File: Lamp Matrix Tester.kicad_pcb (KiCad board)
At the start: 2 copper layers, 50.8 x 53.3 mm, 11 parts, among them J1 Columns, J2 Rows, U1 1088AS

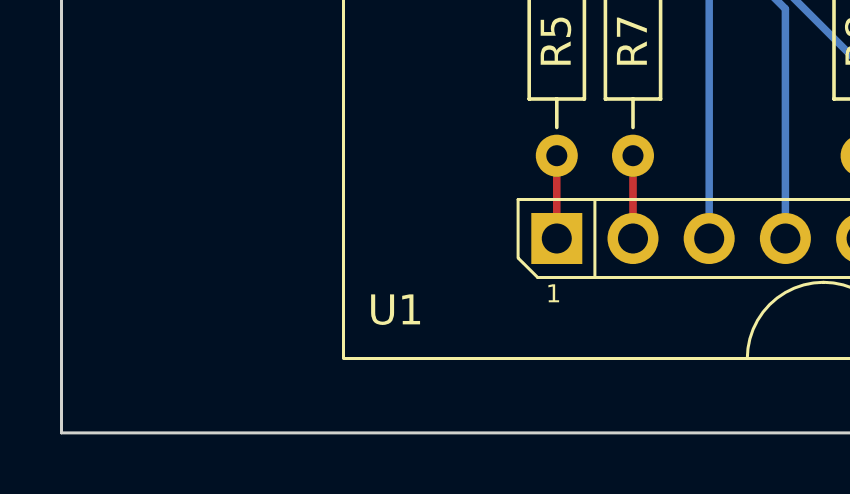
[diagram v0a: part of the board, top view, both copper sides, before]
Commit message: Migrate to Kicad 8 + Included symbol/footprint and 3D model for 1088AS module
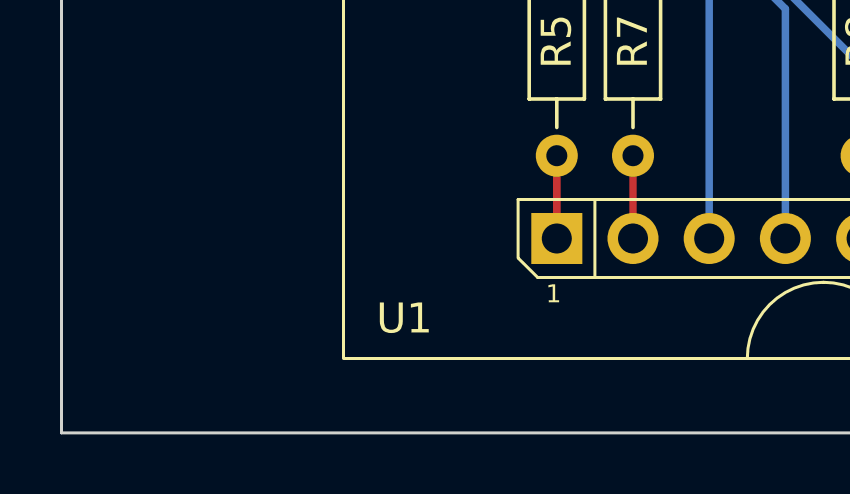
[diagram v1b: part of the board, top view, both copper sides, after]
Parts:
- U1: footprint Library:Led_1088AS_8x8_P2.54mm -> LampMatrixTesterLibrary:Led_1088AS_8x8_P2.54mm
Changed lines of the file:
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@@
     )
   )
-  (footprint "Library:Led_1088AS_8x8_P2.54mm" locked (layer "F.Cu")
+  (footprint "LampMatrixTesterLibrary:Led_1088AS_8x8_P2.54mm" (layer "F.Cu")
     (at 48.26 50.1)
     (descr "8x8 Led matrix module (rows on cathodes)")
@@
     (property "Sheetname" "")
     (attr through_hole)
-    (fp_text reference "U1" (at -14.26 14.4) (layer "F.SilkS")
+    (fp_text reference "U1" (at -13.97 14.67) (layer "F.SilkS")
         (effects (font (size 1 1) (thickness 0.15)))
     )
@@
         (effects (font (size 1 1) (thickness 0.15)))
     )
-    (fp_text user "U1" (at 0 0 180) (layer "F.Fab")
+    (fp_text user "${REFERENCE}" (at 10.16 -17.78 180) (layer "F.Fab")
         (effects (font (size 1 1) (thickness 0.15)))
     )
@@
     (fp_line (start 10.16 13.27) (end -9.525 13.27)
       (stroke (width 0.1) (type solid)) (layer "F.Fab"))
-    (pad "1" thru_hole rect locked (at -8.89 12) (size 1.7 1.7) (drill 1) (layers "*.Cu" "*.Mask")
+    (pad "1" thru_hole rect (at -8.89 12) (size 1.7 1.7) (drill 1) (layers "*.Cu" "*.Mask")
       (net 21 "Net-(U1-R5)") (pinfunction "R5") (pintype "input"))
-    (pad "2" thru_hole oval locked (at -6.35 12) (size 1.7 1.7) (drill 1) (layers "*.Cu" "*.Mask")
+    (pad "2" thru_hole oval (at -6.35 12) (size 1.7 1.7) (drill 1) (layers "*.Cu" "*.Mask")
       (net 23 "Net-(U1-R7)") (pinfunction "R7") (pintype "input"))
-    (pad "3" thru_hole oval locked (at -3.81 12) (size 1.7 1.7) (drill 1) (layers "*.Cu" "*.Mask")
+    (pad "3" thru_hole oval (at -3.81 12) (size 1.7 1.7) (drill 1) (layers "*.Cu" "*.Mask")
       (net 2 "/Col_2") (pinfunction "C2") (pintype "input"))
-    (pad "4" thru_hole oval locked (at -1.27 12) (size 1.7 1.7) (drill 1) (layers "*.Cu" "*.Mask")
+    (pad "4" thru_hole oval (at -1.27 12) (size 1.7 1.7) (drill 1) (layers "*.Cu" "*.Mask")
       (net 3 "/Col_3") (pinfunction "C3") (pintype "input"))
-    (pad "5" thru_hole oval locked (at 1.27 12) (size 1.7 1.7) (drill 1) (layers "*.Cu" "*.Mask")
+    (pad "5" thru_hole oval (at 1.27 12) (size 1.7 1.7) (drill 1) (layers "*.Cu" "*.Mask")
       (net 24 "Net-(U1-R8)") (pinfunction "R8") (pintype "input"))
-    (pad "6" thru_hole oval locked (at 3.81 12) (size 1.7 1.7) (drill 1) (layers "*.Cu" "*.Mask")
+    (pad "6" thru_hole oval (at 3.81 12) (size 1.7 1.7) (drill 1) (layers "*.Cu" "*.Mask")
       (net 5 "/Col_5") (pinfunction "C5") (pintype "input"))
-    (pad "7" thru_hole oval locked (at 6.35 12) (size 1.7 1.7) (drill 1) (layers "*.Cu" "*.Mask")
+    (pad "7" thru_hole oval (at 6.35 12) (size 1.7 1.7) (drill 1) (layers "*.Cu" "*.Mask")
       (net 22 "Net-(U1-R6)") (pinfunction "R6") (pintype "input"))
-    (pad "8" thru_hole oval locked (at 8.89 12) (size 1.7 1.7) (drill 1) (layers "*.Cu" "*.Mask")
+    (pad "8" thru_hole oval (at 8.89 12) (size 1.7 1.7) (drill 1) (layers "*.Cu" "*.Mask")
       (net 19 "Net-(U1-R3)") (pinfunction "R3") (pintype "input"))
-    (pad "9" thru_hole oval locked (at 8.89 -12) (size 1.7 1.7) (drill 1) (layers "*.Cu" "*.Mask")
+    (pad "9" thru_hole oval (at 8.89 -12) (size 1.7 1.7) (drill 1) (layers "*.Cu" "*.Mask")
       (net 17 "Net-(U1-R1)") (pinfunction "R1") (pintype "input"))
-    (pad "10" thru_hole oval locked (at 6.35 -12) (size 1.7 1.7) (drill 1) (layers "*.Cu" "*.Mask")
+    (pad "10" thru_hole oval (at 6.35 -12) (size 1.7 1.7) (drill 1) (layers "*.Cu" "*.Mask")
       (net 4 "/Col_4") (pinfunction "C4") (pintype "input"))
-    (pad "11" thru_hole oval locked (at 3.81 -12) (size 1.7 1.7) (drill 1) (layers "*.Cu" "*.Mask")
+    (pad "11" thru_hole oval (at 3.81 -12) (size 1.7 1.7) (drill 1) (layers "*.Cu" "*.Mask")
       (net 6 "/Col_6") (pinfunction "C6") (pintype "input"))
-    (pad "12" thru_hole oval locked (at 1.27 -12) (size 1.7 1.7) (drill 1) (layers "*.Cu" "*.Mask")
+    (pad "12" thru_hole oval (at 1.27 -12) (size 1.7 1.7) (drill 1) (layers "*.Cu" "*.Mask")
       (net 20 "Net-(U1-R4)") (pinfunction "R4") (pintype "input"))
-    (pad "13" thru_hole oval locked (at -1.27 -12) (size 1.7 1.7) (drill 1) (layers "*.Cu" "*.Mask")
+    (pad "13" thru_hole oval (at -1.27 -12) (size 1.7 1.7) (drill 1) (layers "*.Cu" "*.Mask")
       (net 1 "/Col_1") (pinfunction "C1") (pintype "input"))
-    (pad "14" thru_hole oval locked (at -3.81 -12) (size 1.7 1.7) (drill 1) (layers "*.Cu" "*.Mask")
+    (pad "14" thru_hole oval (at -3.81 -12) (size 1.7 1.7) (drill 1) (layers "*.Cu" "*.Mask")
       (net 18 "Net-(U1-R2)") (pinfunction "R2") (pintype "input"))
-    (pad "15" thru_hole oval locked (at -6.35 -12) (size 1.7 1.7) (drill 1) (layers "*.Cu" "*.Mask")
+    (pad "15" thru_hole oval (at -6.35 -12) (size 1.7 1.7) (drill 1) (layers "*.Cu" "*.Mask")
       (net 7 "/Col_7") (pinfunction "C7") (pintype "input"))
-    (pad "16" thru_hole oval locked (at -8.89 -12) (size 1.7 1.7) (drill 1) (layers "*.Cu" "*.Mask")
+    (pad "16" thru_hole oval (at -8.89 -12) (size 1.7 1.7) (drill 1) (layers "*.Cu" "*.Mask")
       (net 8 "/Col_8") (pinfunction "C8") (pintype "input"))
-    (group "" (id c3c0f99f-4d0d-44f3-8ddc-d9922da41b62)
+    (group "" (id a1a837f2-3108-4928-a6f4-b132db4ccddd)
       (members
-        1d42fcd8-2e62-4ff4-bf4f-0d9796c08360
-        225f8b9c-66c4-40d9-9750-5710a2363b21
-        8537e2e2-14ee-4543-85dc-780dc662be52
-        ac02bdee-bd3c-4e5c-b07d-a869ff1d9e67
-        ae8fa927-c6e5-473f-b426-9e538e204b24
-        c94030db-bb61-4ea9-8f4f-ef515706781c
-        d024c547-cc7a-4b46-b0f6-59b0b7fc992f
-        e02f33ed-c537-44ce-9ee1-47ec356ef4e5
+        1cf74098-5c5e-48d5-85f0-7177242f448c
+        3dd3e696-4dba-49ff-b819-33acb4febae2
+        7f8723ab-5faa-487d-affa-12158fbca0bc
+        a025b1e1-c8fe-4855-98e9-898110f67208
+        cbbb2db2-bd63-44f0-985e-de75ed6dc4bf
+        dd6336c7-fc82-47f6-a3b7-e740f6896745
+        f3c5d8a2-d138-49cd-ae26-8cfcbbe5acf6
+        f6986f73-316d-43d9-8db3-c2306fb82dc4
       )
     )
-    (group "" (id fc83c96c-165a-4660-b6a9-d018e09fc072)
+    (group "" (id 9c16a829-b1ab-49b2-98e5-687f221d9bf0)
       (members
-        13a8d455-e565-41d1-b409-6f24af8a4f9f
-        4ede1359-be1e-4ba4-808c-ab1266c04e3e
-        50e66003-7959-4cb0-80fd-75a62432dae1
-        679702f1-175e-4411-b736-8f39248482f7
-        6ad50209-8828-4da2-84b9-7d5396c3b7e7
-        7665fbbf-e485-4393-ab95-2a9e2f6412e3
-        abba2eec-ea96-495b-8fc0-f119f6824fec
-        f749e732-3b04-4a25-9612-401c73e91e84
+        12a68be6-d721-4ca3-ad30-b288c09ac475
+        1721b806-7056-450d-8de7-e5958fba88a5
+        acb6f0c7-c9bd-4d54-8549-eaaffdf5ae6c
+        bd9d33ee-aea6-49ac-ba29-9b97fb06abf9
+        beafbfd6-5118-4f2e-b5b0-375d07ac19cd
+        dd904018-ee36-4d4f-b77a-113e29d64020
+        ee5f0afc-288a-453e-9e07-d4185b3ebcbb
+        eeef8bb1-48df-4290-b8f9-6b7b358dfeef
       )
     )
-    (model "${KICAD6_3DMODEL_DIR}/Connector_PinHeader_2.54mm.3dshapes/PinHeader_1x16_P2.54mm_Vertical.wrl" hide
+    (model "${KIPRJMOD}/libs/Models/1088ASBS.step"
       (offset (xyz 0 0 0))
       (scale (xyz 1 1 1))
